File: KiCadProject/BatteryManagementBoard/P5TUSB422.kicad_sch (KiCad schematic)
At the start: 6 parts, among them U402 TUSB422

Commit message: Tweaking
Signed-off-by: Eldalote.Electronics <Eldalote.Electronics@gmail.com>
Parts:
- C501: renamed from C404; footprint (none) -> Capacitor_SMD:C_0805_2012Metric
- C502: renamed from C405; footprint (none) -> Capacitor_SMD:C_0603_1608Metric
- C503: renamed from C406; footprint (none) -> Capacitor_SMD:C_0402_1005Metric
- C504: renamed from C407; footprint (none) -> Capacitor_SMD:C_0402_1005Metric
- R501: renamed from R401; footprint (none) -> Resistor_SMD:R_0402_1005Metric
- renumbered U402 to U501
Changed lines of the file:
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@@
     (effects (font (size 1.27 1.27)) (justify left bottom))
   )
-  (label "INT_N" (at 180.34 83.82 180)
+  (label "TUS_INT_N" (at 180.34 83.82 180)
     (effects (font (size 1.27 1.27)) (justify right bottom))
   )
@@
     (effects (font (size 1.27 1.27)) (justify right bottom))
   )
-  (label "INT_N" (at 38.1 160.02 0)
+  (label "TUS_INT_N" (at 38.1 160.02 0)
     (effects (font (size 1.27 1.27)) (justify left bottom))
   )
@@
   (symbol (lib_id "Device:C") (at 162.56 104.14 0) (unit 1)
     (in_bom yes) (on_board yes)
-    (property "Reference" "C406" (id 0) (at 163.83 101.6 0)
+    (property "Reference" "C503" (id 0) (at 163.83 101.6 0)
       (effects (font (size 1.27 1.27)) (justify left))
     )
@@
       (effects (font (size 1.27 1.27)) (justify left))
     )
-    (property "Footprint" "" (id 2) (at 163.5252 107.95 0)
+    (property "Footprint" "Capacitor_SMD:C_0402_1005Metric" (id 2) (at 163.5252 107.95 0)
       (effects (font (size 1.27 1.27)) hide)
     )
@@
   (symbol (lib_id "Device:C") (at 172.72 104.14 0) (unit 1)
     (in_bom yes) (on_board yes)
-    (property "Reference" "C407" (id 0) (at 173.99 101.6 0)
+    (property "Reference" "C504" (id 0) (at 173.99 101.6 0)
       (effects (font (size 1.27 1.27)) (justify left))
     )
@@
       (effects (font (size 1.27 1.27)) (justify left))
     )
-    (property "Footprint" "" (id 2) (at 173.6852 107.95 0)
+    (property "Footprint" "Capacitor_SMD:C_0402_1005Metric" (id 2) (at 173.6852 107.95 0)
       (effects (font (size 1.27 1.27)) hide)
     )
@@
   (symbol (lib_id "Eldalote_symbols:TUSB422") (at 146.05 91.44 0) (unit 1)
     (in_bom yes) (on_board yes) (fields_autoplaced)
-    (property "Reference" "U402" (id 0) (at 148.0694 72.39 0)
+    (property "Reference" "U501" (id 0) (at 148.0694 72.39 0)
       (effects (font (size 1.27 1.27)) (justify left))
     )
@@
   (symbol (lib_id "power:VBUS") (at 128.27 71.12 0) (unit 1)
     (in_bom yes) (on_board yes) (fields_autoplaced)
-    (property "Reference" "#PWR0402" (id 0) (at 128.27 74.93 0)
+    (property "Reference" "#PWR0502" (id 0) (at 128.27 74.93 0)
       (effects (font (size 1.27 1.27)) hide)
     )
@@
   (symbol (lib_id "power:GND") (at 146.05 119.38 0) (unit 1)
     (in_bom yes) (on_board yes) (fields_autoplaced)
-    (property "Reference" "#PWR0403" (id 0) (at 146.05 125.73 0)
+    (property "Reference" "#PWR0503" (id 0) (at 146.05 125.73 0)
       (effects (font (size 1.27 1.27)) hide)
     )
@@
   (symbol (lib_id "power:GND") (at 153.67 69.85 0) (unit 1)
     (in_bom yes) (on_board yes) (fields_autoplaced)
-    (property "Reference" "#PWR0405" (id 0) (at 153.67 76.2 0)
+    (property "Reference" "#PWR0505" (id 0) (at 153.67 76.2 0)
       (effects (font (size 1.27 1.27)) hide)
     )
@@
   (symbol (lib_id "Device:R") (at 176.53 74.93 0) (unit 1)
     (in_bom yes) (on_board yes) (fields_autoplaced)
-    (property "Reference" "R401" (id 0) (at 179.07 73.6599 0)
+    (property "Reference" "R501" (id 0) (at 179.07 73.6599 0)
       (effects (font (size 1.27 1.27)) (justify left))
     )
@@
       (effects (font (size 1.27 1.27)) (justify left))
     )
-    (property "Footprint" "" (id 2) (at 174.752 74.93 90)
+    (property "Footprint" "Resistor_SMD:R_0402_1005Metric" (id 2) (at 174.752 74.93 90)
       (effects (font (size 1.27 1.27)) hide)
     )
@@
   (symbol (lib_id "Device:C") (at 153.67 64.77 0) (unit 1)
     (in_bom yes) (on_board yes)
-    (property "Reference" "C405" (id 0) (at 154.94 62.23 0)
+    (property "Reference" "C502" (id 0) (at 154.94 62.23 0)
       (effects (font (size 1.27 1.27)) (justify left))
     )
@@
       (effects (font (size 1.27 1.27)) (justify left))
     )
-    (property "Footprint" "" (id 2) (at 154.6352 68.58 0)
+    (property "Footprint" "Capacitor_SMD:C_0603_1608Metric" (id 2) (at 154.6352 68.58 0)
       (effects (font (size 1.27 1.27)) hide)
     )
@@
   (symbol (lib_id "Device:C") (at 120.65 81.28 0) (unit 1)
     (in_bom yes) (on_board yes)
-    (property "Reference" "C404" (id 0) (at 121.92 78.74 0)
+    (property "Reference" "C501" (id 0) (at 121.92 78.74 0)
       (effects (font (size 1.27 1.27)) (justify left))
     )
@@
       (effects (font (size 1.27 1.27)) (justify left))
     )
-    (property "Footprint" "" (id 2) (at 121.6152 85.09 0)
+    (property "Footprint" "Capacitor_SMD:C_0805_2012Metric" (id 2) (at 121.6152 85.09 0)
       (effects (font (size 1.27 1.27)) hide)
     )
@@
   (symbol (lib_id "power:GND") (at 120.65 87.63 0) (unit 1)
     (in_bom yes) (on_board yes) (fields_autoplaced)
-    (property "Reference" "#PWR0401" (id 0) (at 120.65 93.98 0)
+    (property "Reference" "#PWR0501" (id 0) (at 120.65 93.98 0)
       (effects (font (size 1.27 1.27)) hide)
     )
@@
   (symbol (lib_id "power:+3.3V") (at 151.13 58.42 0) (unit 1)
     (in_bom yes) (on_board yes) (fields_autoplaced)
-    (property "Reference" "#PWR0404" (id 0) (at 151.13 62.23 0)
-      (effects (font (size 1.27 1.27)) hide)
-    )
+    (property "Reference" "#PWR0504" (id 0) (at 151.13 62.23 0)
+      (effects (font (size 1.27 1.27)) hide)
+    )

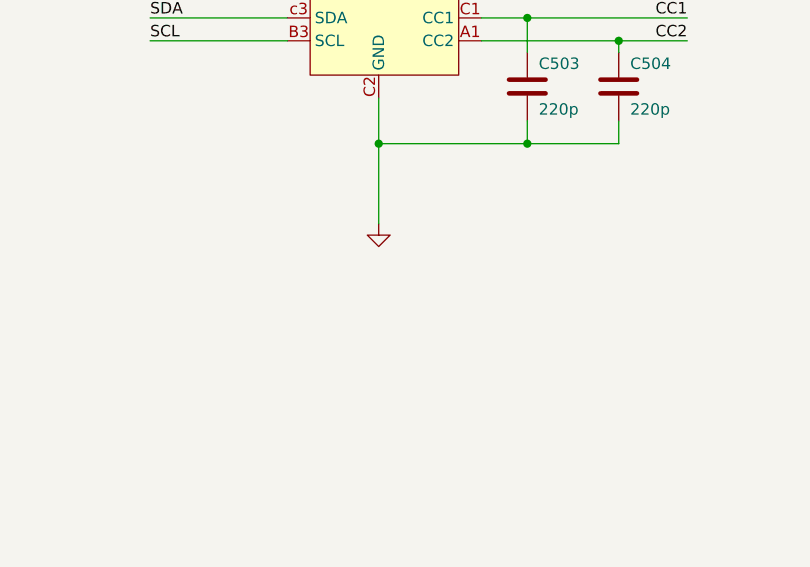
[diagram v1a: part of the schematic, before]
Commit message: Final touches before component order and PCB layout
Signed-off-by: Eldalote.Electronics <Eldalote.Electronics@gmail.com>
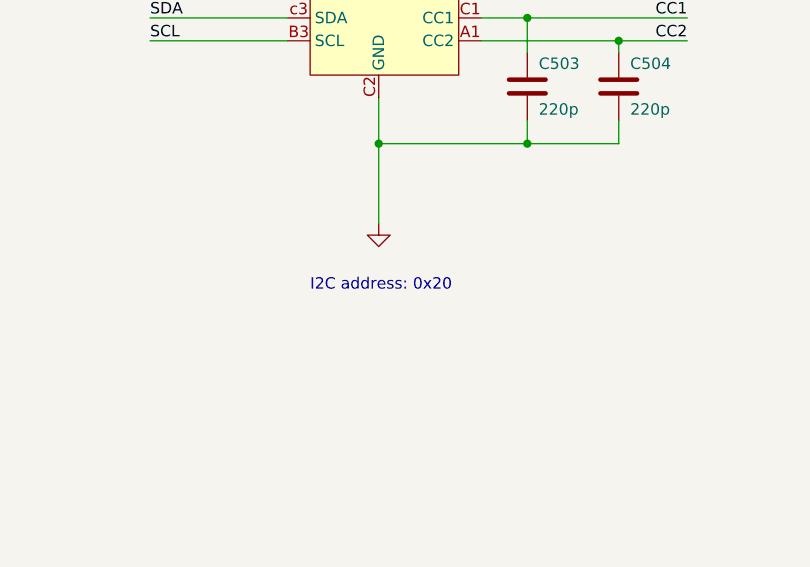
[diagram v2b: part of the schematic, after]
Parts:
- U501: footprint (none) -> Package_BGA:Texas_DSBGA-9_1.4715x1.4715mm_Layout3x3_P0.5mm
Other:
- note added: "I2C address: 0x20"
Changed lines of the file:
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@@
     (stroke (width 0) (type default) (color 0 0 0 0))
+  )
+  (text "I2C address: 0x20" (at 138.43 127 0)
+    (effects (font (size 1.27 1.27)) (justify left bottom))
   )
   (text "All components on this page are optional, DNP initially\n"
@@
       (effects (font (size 1.27 1.27)) (justify left))
     )
-    (property "Footprint" "" (id 2) (at 146.05 91.44 0)
+    (property "Footprint" "Package_BGA:Texas_DSBGA-9_1.4715x1.4715mm_Layout3x3_P0.5mm" (id 2) (at 146.05 91.44 0)
       (effects (font (size 1.27 1.27)) hide)
     )

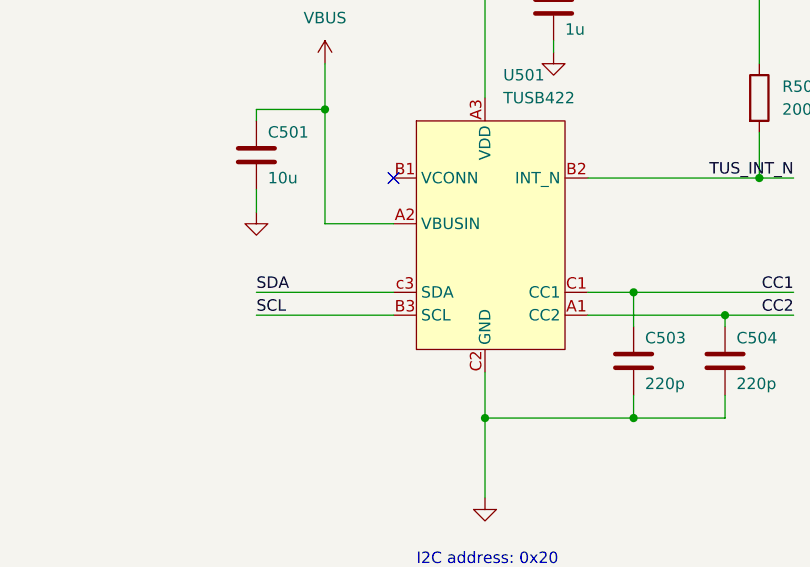
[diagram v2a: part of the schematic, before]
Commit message: Components selected, MfID added to schematics, and components ordered
Signed-off-by: Eldalote.Electronics <Eldalote.Electronics@gmail.com>
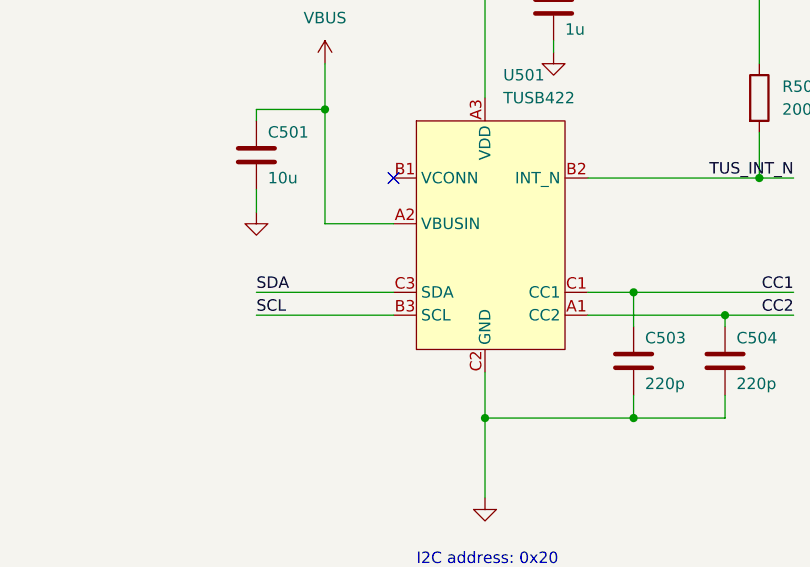
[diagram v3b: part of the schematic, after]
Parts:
- C501: Extra Requirement (none) -> 25V; MfID (none) -> CL21A106KAYNNNG
- C502: Extra Requirement (none) -> 25V; MfID (none) -> CL10A105KA8NNNC
- C503, C504: MfID (none) -> 885012205057
- R501: MfID (none) -> CR0402-FX-2003GLF
- U501: MfID (none) -> TUSB422IYFPR
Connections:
- net SDA: now also U501.C3 (SDA); no longer U501.c3 (SDA)
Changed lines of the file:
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@@
+      (effects (font (size 1.27 1.27)) hide)
+    )
+    (property "MfID" "885012205057" (id 4) (at 162.56 104.14 0)
       (effects (font (size 1.27 1.27)) hide)
     )
@@
       (effects (font (size 1.27 1.27)) hide)
     )
+    (property "MfID" "885012205057" (id 4) (at 172.72 104.14 0)
+      (effects (font (size 1.27 1.27)) hide)
+    )
     (pin "1")
     (pin "2")
@@
       (effects (font (size 1.27 1.27)) hide)
     )
+    (property "MfID" "TUSB422IYFPR" (id 4) (at 146.05 91.44 0)
+      (effects (font (size 1.27 1.27)) hide)
+    )
     (pin "A1")
     (pin "A2")
@@
     (pin "C1")
     (pin "C2")
-    (pin "c3")
+    (pin "C3")
   )
   (symbol (lib_id "power:VBUS") (at 128.27 71.12 0) (unit 1)
@@
       (effects (font (size 1.27 1.27)) hide)
     )
+    (property "MfID" "CR0402-FX-2003GLF" (id 4) (at 176.53 74.93 0)
+      (effects (font (size 1.27 1.27)) hide)
+    )
     (pin "1")
     (pin "2")
@@
     )
     (property "Datasheet" "~" (id 3) (at 153.67 64.77 0)
+      (effects (font (size 1.27 1.27)) hide)
+    )
+    (property "Extra Requirement" "25V" (id 4) (at 153.67 64.77 0)
+      (effects (font (size 1.27 1.27)) hide)
+    )
+    (property "MfID" "CL10A105KA8NNNC" (id 5) (at 153.67 64.77 0)
       (effects (font (size 1.27 1.27)) hide)
     )
@@
       (effects (font (size 1.27 1.27)) hide)
     )
+    (property "Extra Requirement" "25V" (id 4) (at 120.65 81.28 0)
+      (effects (font (size 1.27 1.27)) hide)
+    )
+    (property "MfID" "CL21A106KAYNNNG" (id 5) (at 120.65 81.28 0)
+      (effects (font (size 1.27 1.27)) hide)
+    )

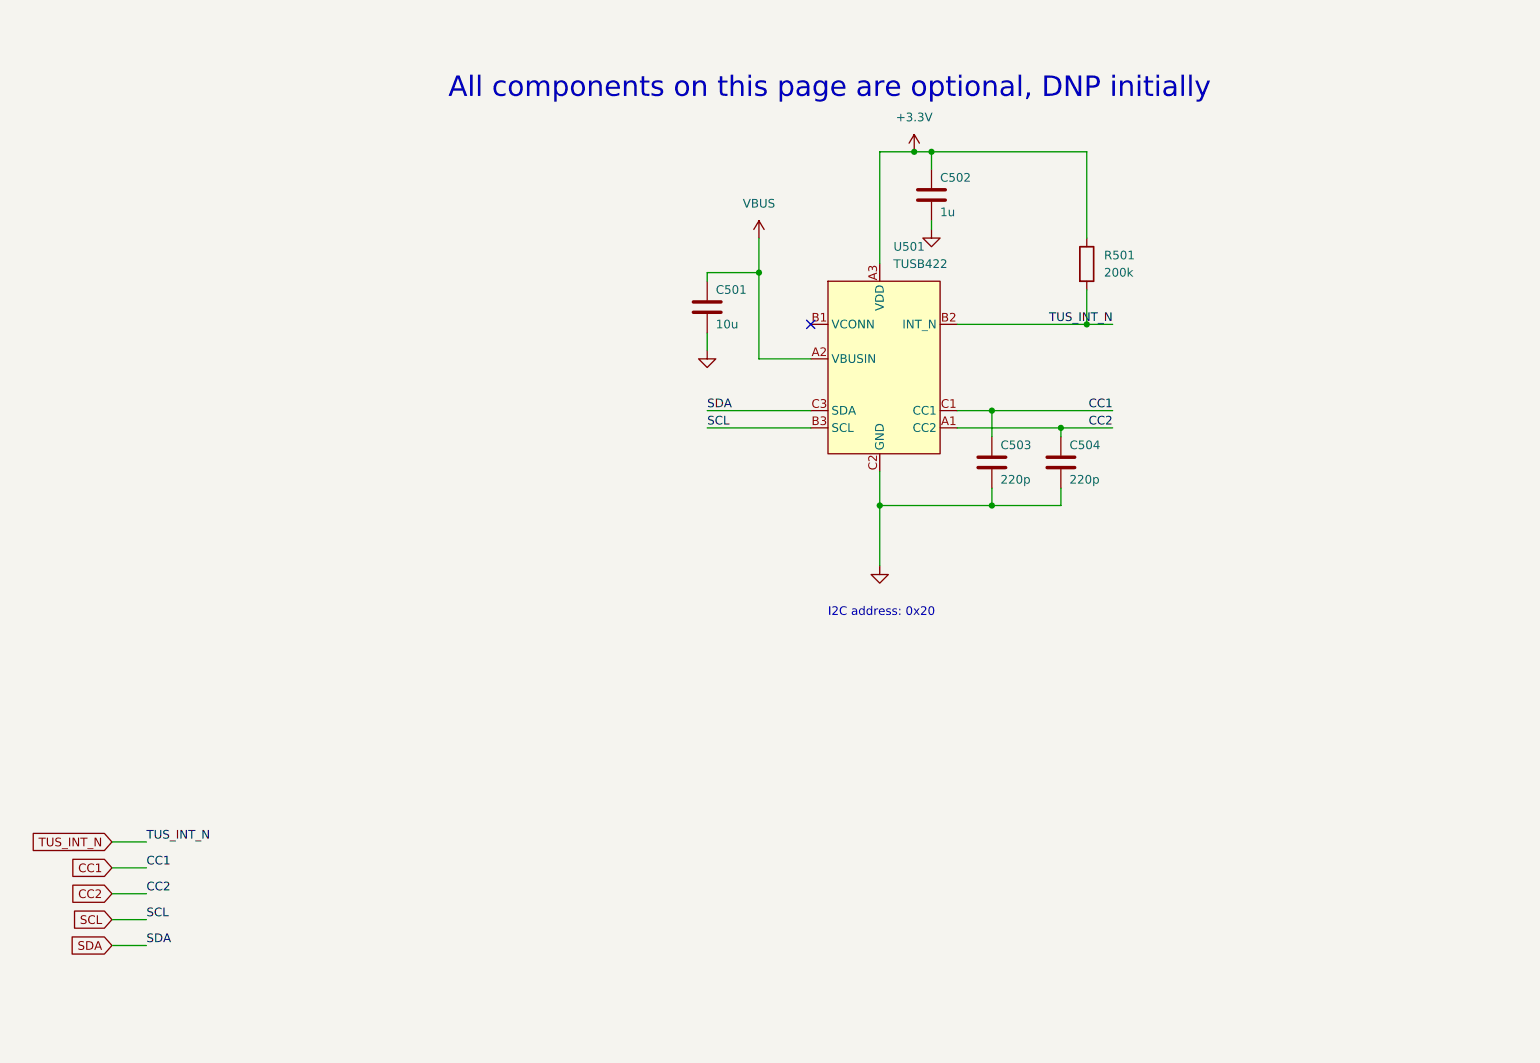
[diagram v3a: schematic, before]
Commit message: Routed Bat management (replaced TUSB because it physically can't be routed with constraints)
Signed-off-by: Eldalote.Electronics <Eldalote.Electronics@gmail.com>
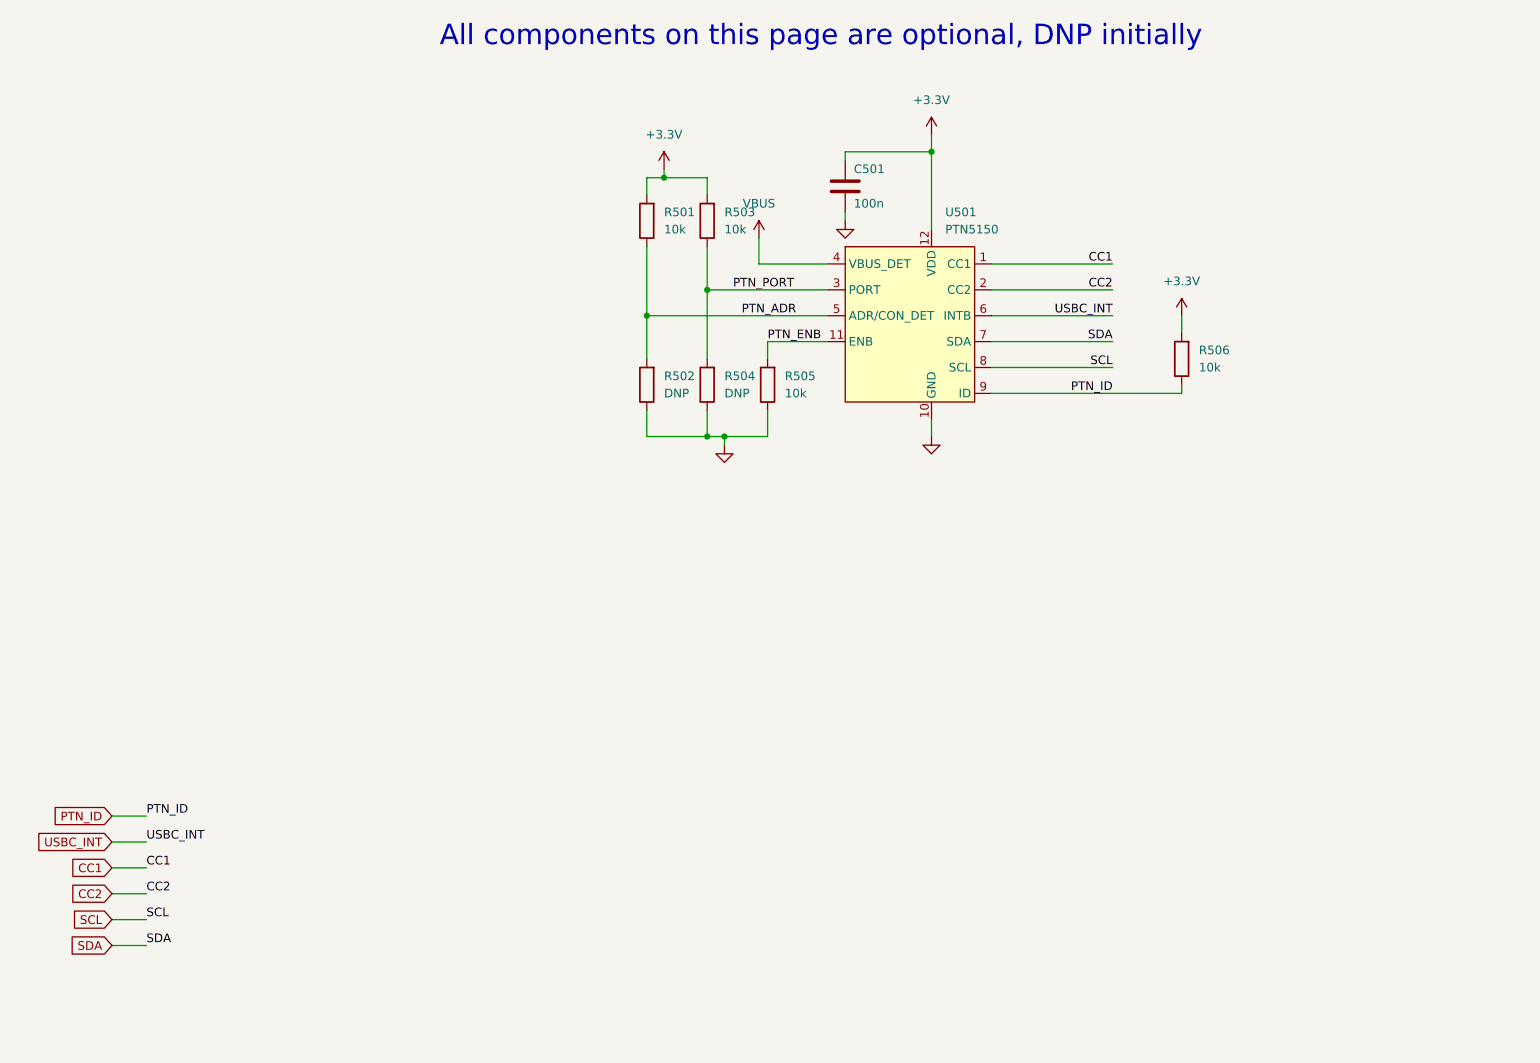
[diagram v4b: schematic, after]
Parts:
- removed C502: 1u, Capacitor_SMD:C_0603_1608Metric, symbol Device:C
- removed C503, C504: 220p, Capacitor_SMD:C_0402_1005Metric, symbol Device:C
- removed U501: TUSB422, Package_BGA:Texas_DSBGA-9_1.4715x1.4715mm_Layout3x3_P0.5mm, symbol Eldalote_symbols:TUSB422
- added R502, R504: DNP, Resistor_SMD:R_0402_1005Metric, symbol Device:R
- added R503, R505, R506: 10k, Resistor_SMD:R_0402_1005Metric, symbol Device:R
- added U501: PTN5150, Package_DFN_QFN:Texas_X2QFN-12_1.6x1.6mm_P0.4mm, symbol Eldalote_symbols:PTN5150
- C501: value 10u -> 100n; footprint Capacitor_SMD:C_0805_2012Metric -> Capacitor_SMD:C_0402_1005Metric; MfID CL21A106KAYNNNG -> CL05A104KA5NNNC
- R501: value 200k -> 10k; MfID CR0402-FX-2003GLF -> CR0402-FX-1002GLF
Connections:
- net TUS_INT_N is gone; now on net +3.3V: R501.2
- net +3.3V: now also C501.1, R503.2, R506.2, U501.12 (VDD); no longer R501.1
- net CC1: now also U501.1 (CC1)
- net CC2: now also U501.2 (CC2)
- net GND: now also R502.1, R504.1, R505.1, U501.10 (GND)
- net SCL: now also U501.8 (SCL)
- net SDA: now also U501.7 (SDA)
- net VBUS: now also U501.4 (VBUS_DET); no longer C501.1
- new net PTN_ADR: R501.1, R502.2, U501.5 (ADR/CON_DET)
- new net PTN_ENB: R505.2, U501.11 (ENB)
- new net PTN_ID: R506.1, U501.9 (ID)
- new net PTN_PORT: R503.1, R504.2, U501.3 (PORT)
- new net USBC_INT: U501.6 (INTB)
- no-connect marks 1 -> 0
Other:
- note removed: "I2C address: 0x20"
